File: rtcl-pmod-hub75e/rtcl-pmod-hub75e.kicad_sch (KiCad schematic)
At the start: 18 parts, among them J1 PMOD, J2 HIF3FC-16PA-2.54DSA(71), U1 74LVC273, U2 74LVC273, U3 74LVC273, U4 74LVC273, U5 LM809M3-2.93, U6 74LVC2G86

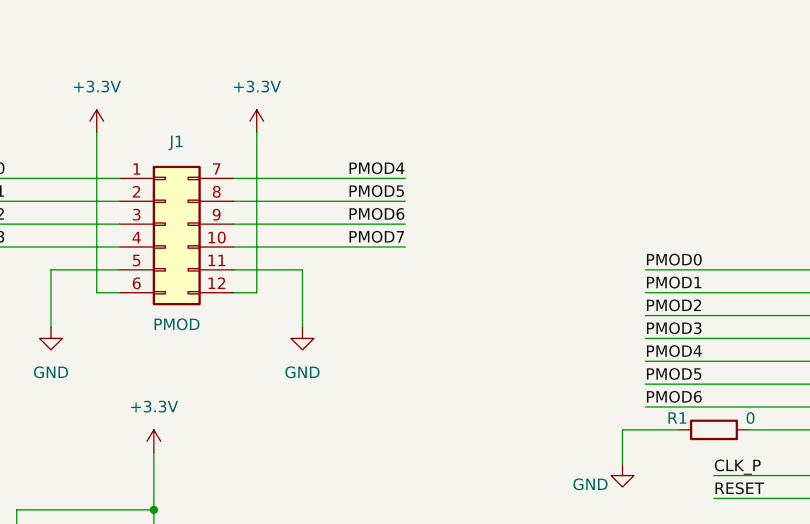
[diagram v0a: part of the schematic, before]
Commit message: Update .gitignore and modify schematic for power symbols and designators
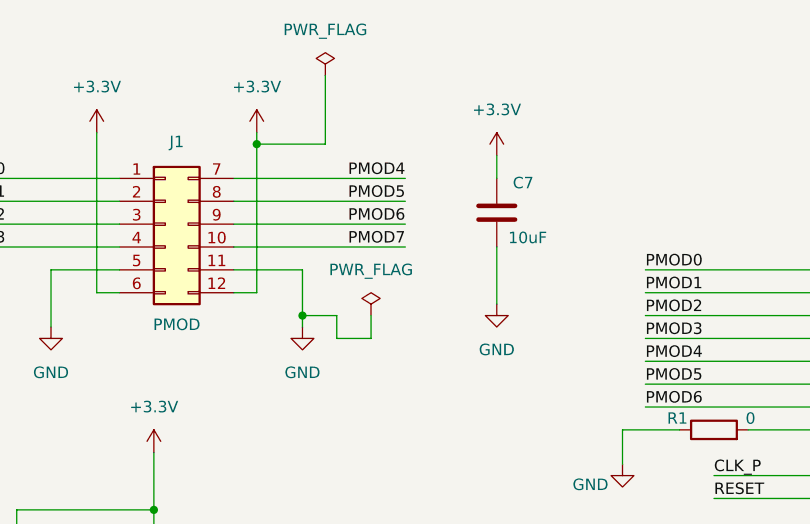
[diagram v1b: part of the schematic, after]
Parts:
- added C7: 10uF, symbol Device:C
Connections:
- net +3.3V: now also C7.1
- net GND: now also C7.2

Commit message: Add footprints for PH_02x06_2.54mm and PH_02x08_2.54mm headers; update existing schematic properties
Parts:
- C1, C2, C3, C4, C5, C6, C7: footprint (none) -> Capacitor_SMD:C_0603_1608Metric
- J1: footprint (none) -> rtcl-pmod-hub75e:PH_02x06_2.54mm
- J2: footprint (none) -> rtcl-pmod-hub75e:PH_02x08_2.54mm
- R1, R2: footprint (none) -> Resistor_SMD:R_0603_1608Metric
- TP1, TP2: footprint (none) -> TestPoint:TestPoint_Pad_2.0x2.0mm
- U1, U2, U3, U4: footprint (none) -> Package_SO:TSSOP-20_4.4x6.5mm_P0.65mm
- U5: LCSC (none) -> C414611
- U6: footprint (none) -> Package_SO:VSSOP-8_2.3x2mm_P0.5mm; LCSC (none) -> C507252
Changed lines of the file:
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@@
 			)
 		)
-		(property "Footprint" ""
+		(property "Footprint" "Package_SO:TSSOP-20_4.4x6.5mm_P0.65mm"
 			(at 181.61 129.54 0)
 			(hide yes)
@@
 			)
 		)
-		(property "Footprint" ""
+		(property "Footprint" "Resistor_SMD:R_0603_1608Metric"
 			(at 111.76 136.398 90)
 			(hide yes)
@@
 			)
 		)
-		(property "Footprint" ""
+		(property "Footprint" "TestPoint:TestPoint_Pad_2.0x2.0mm"
 			(at 207.01 134.62 0)
 			(hide yes)
@@
 			)
 		)
-		(property "Footprint" ""
+		(property "Footprint" "Package_SO:TSSOP-20_4.4x6.5mm_P0.65mm"
 			(at 137.16 129.54 0)
 			(hide yes)
@@
 			)
 		)
-		(property "Footprint" ""
+		(property "Footprint" "Package_SO:TSSOP-20_4.4x6.5mm_P0.65mm"
 			(at 181.61 60.96 0)
 			(hide yes)
@@
 			)
 		)
-		(property "Footprint" ""
+		(property "Footprint" "Capacitor_SMD:C_0603_1608Metric"
 			(at 130.5052 107.95 0)
 			(hide yes)
@@
 			)
 		)
-		(property "Footprint" ""
+		(property "Footprint" "Capacitor_SMD:C_0603_1608Metric"
 			(at 174.9552 39.37 0)
 			(hide yes)
@@
 			)
 		)
-		(property "Footprint" ""
+		(property "Footprint" "Capacitor_SMD:C_0603_1608Metric"
 			(at 174.9552 107.95 0)
 			(hide yes)
@@
 			)
 		)
-		(property "Footprint" ""
+		(property "Footprint" "Package_SO:TSSOP-20_4.4x6.5mm_P0.65mm"
 			(at 137.16 60.96 0)
 			(hide yes)
@@
 			)
 		)
-		(property "Footprint" ""
+		(property "Footprint" "Capacitor_SMD:C_0603_1608Metric"
 			(at 36.5252 135.89 0)
 			(hide yes)
@@
 			)
 		)
+		(property "LCSC" "C414611"
+			(at 50.8 90.17 0)
+			(hide yes)
+			(show_name no)
+			(do_not_autoplace no)
+			(effects
+				(font
+					(size 1.27 1.27)
+				)
+			)
+		)
 		(pin "3"
 		)
@@
 			)
 		)
-		(property "Footprint" ""
+		(property "Footprint" "Package_SO:VSSOP-8_2.3x2mm_P0.5mm"
 			(at 83.82 185.42 0)
 			(hide yes)
@@
 			)
 		)
+		(property "LCSC" "C507252"
+			(at 83.82 185.42 0)
+			(hide yes)
+			(show_name no)
+			(do_not_autoplace no)
+			(effects
+				(font
+					(size 1.27 1.27)
+				)
+			)
+		)
 		(pin "6"
 		)
@@
 			)
 		)
-		(property "Footprint" ""
+		(property "Footprint" "Capacitor_SMD:C_0603_1608Metric"
 			(at 89.8652 45.72 0)
 			(hide yes)
@@
 			)
 		)
-		(property "Footprint" ""
+		(property "Footprint" "Capacitor_SMD:C_0603_1608Metric"
 			(at 36.5252 87.63 0)
 			(hide yes)
@@
 			)
 		)
-		(property "Footprint" ""
+		(property "Footprint" "Package_SO:VSSOP-8_2.3x2mm_P0.5mm"
 			(at 50.8 135.89 0)
 			(hide yes)
@@
 			)
 		)
+		(property "LCSC" "C507252"
+			(at 50.8 135.89 0)
+			(hide yes)
+			(show_name no)
+			(do_not_autoplace no)
+			(effects
+				(font
+					(size 1.27 1.27)
+				)
+			)
+		)
 		(pin "6"
 		)
@@
 			)
 		)
-		(property "Footprint" ""
+		(property "Footprint" "Resistor_SMD:R_0603_1608Metric"
 			(at 113.03 67.818 90)
 			(hide yes)
@@
 			)
 		)
-		(property "Footprint" ""
+		(property "Footprint" "Capacitor_SMD:C_0603_1608Metric"
 			(at 130.5052 39.37 0)
 			(hide yes)
@@
 			)
 		)
-		(property "Footprint" ""
+		(property "Footprint" "TestPoint:TestPoint_Pad_2.0x2.0mm"
 			(at 207.01 66.04 0)
 			(hide yes)
@@
 			)
 		)
-		(property "Footprint" ""
+		(property "Footprint" "Package_SO:VSSOP-8_2.3x2mm_P0.5mm"
 			(at 83.82 168.91 0)
 			(hide yes)
@@
 			)
 		)
+		(property "LCSC" "C507252"
+			(at 83.82 168.91 0)
+			(hide yes)
+			(show_name no)
+			(do_not_autoplace no)
+			(effects
+				(font
+					(size 1.27 1.27)
+				)
+			)
+		)
 		(pin "2"
 		)
@@
 			)
 		)
-		(property "Footprint" ""
+		(property "Footprint" "rtcl-pmod-hub75e:PH_02x08_2.54mm"
 			(at 241.3 92.71 0)
 			(hide yes)
@@
 			)
 		)
-		(property "Footprint" ""
+		(property "Footprint" "rtcl-pmod-hub75e:PH_02x06_2.54mm"
 			(at 52.07 43.18 0)
 			(hide yes)

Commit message: Refactor code structure for improved readability and maintainability
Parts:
- removed TP1, TP2: Conn_01x01, TestPoint:TestPoint_Pad_2.0x2.0mm, symbol Connector_Generic:Conn_01x01
- added J3: Conn_01x02, Connector_PinHeader_2.54mm:PinHeader_1x02_P2.54mm_Vertical, symbol Connector_Generic:Conn_01x02
- added TP1, TP2, TP3, TP4: TestPoint, TestPoint:TestPoint_Pad_D1.0mm, symbol Connector:TestPoint
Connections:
- net +3.3V: now also J3.1 (Pin_1)
- net GND: now also J3.2 (Pin_2)
- net PMOD0: now also U2.8 (D3); no longer U2.3 (D0)
- net PMOD1: now also U2.7 (D2); no longer U2.4 (D1)
- net PMOD2: now also U2.4 (D1); no longer U2.7 (D2)
- net PMOD3: now also U2.3 (D0); no longer U2.8 (D3)
- net PMOD4: now also U1.17 (D6); no longer U1.13 (D4)
- net PMOD6: now also U1.13 (D4); no longer U1.17 (D6)
- net D4N: now reaches U2.12 (Q4), U4.13 (D4)
- net D5N: now reaches U2.15 (Q5), U4.14 (D5)
- net D6N: now reaches U2.16 (Q6), U4.17 (D6)
- net D7N: now reaches U2.19 (Q7), U4.18 (D7)
- net at U4.19 (Q7): now also TP2.1
- net D0N: now reaches U2.2 (Q0), U4.3 (D0)
- net D1N: now reaches U2.5 (Q1), U4.4 (D1)
- net D2N: now reaches U2.6 (Q2), U4.7 (D2)
- net D3N: now reaches U2.9 (Q3), U4.8 (D3)
- net at R2.2, U2.18 (D7): now also TP4.1
- net D4P: now reaches U1.12 (Q4), U3.13 (D4)
- net D5P: now reaches U1.15 (Q5), U3.14 (D5)
- net D6P: now reaches U1.16 (Q6), U3.17 (D6)
- net D7P: now reaches U1.19 (Q7), U3.18 (D7)
- net at U3.19 (Q7): now also TP1.1
- net D0P: now reaches U1.2 (Q0), U3.3 (D0)
- net D1P: now reaches U1.5 (Q1), U3.4 (D1)
- net D2P: now reaches U1.6 (Q2), U3.7 (D2)
- net D3P: now reaches U1.9 (Q3), U3.8 (D3)
- net at R1.2, U1.18 (D7): now also TP3.1
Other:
- moved on the sheet: C3, C4, J2, R1, U3, U4

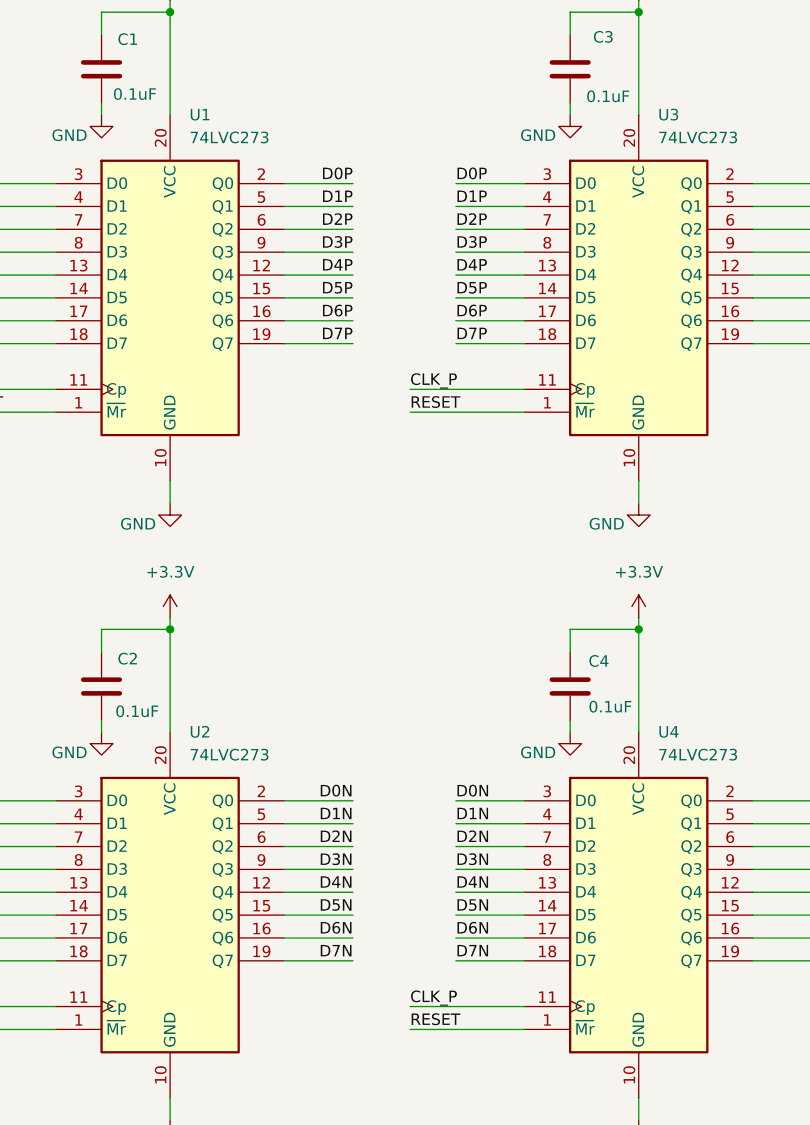
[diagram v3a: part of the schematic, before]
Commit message: Update PCB design parameters and wire connections in the rtcl-pmod-hub75e project
- Changed active layer from 0 to 2 in the project settings.
- Cleared used designators in the project file for better clarity.
- Adjusted multiple wire connection points in the schematic to correct coordinates for improved layout.
- Updated label positions for various components to reflect new wire connections and ensure proper alignment.
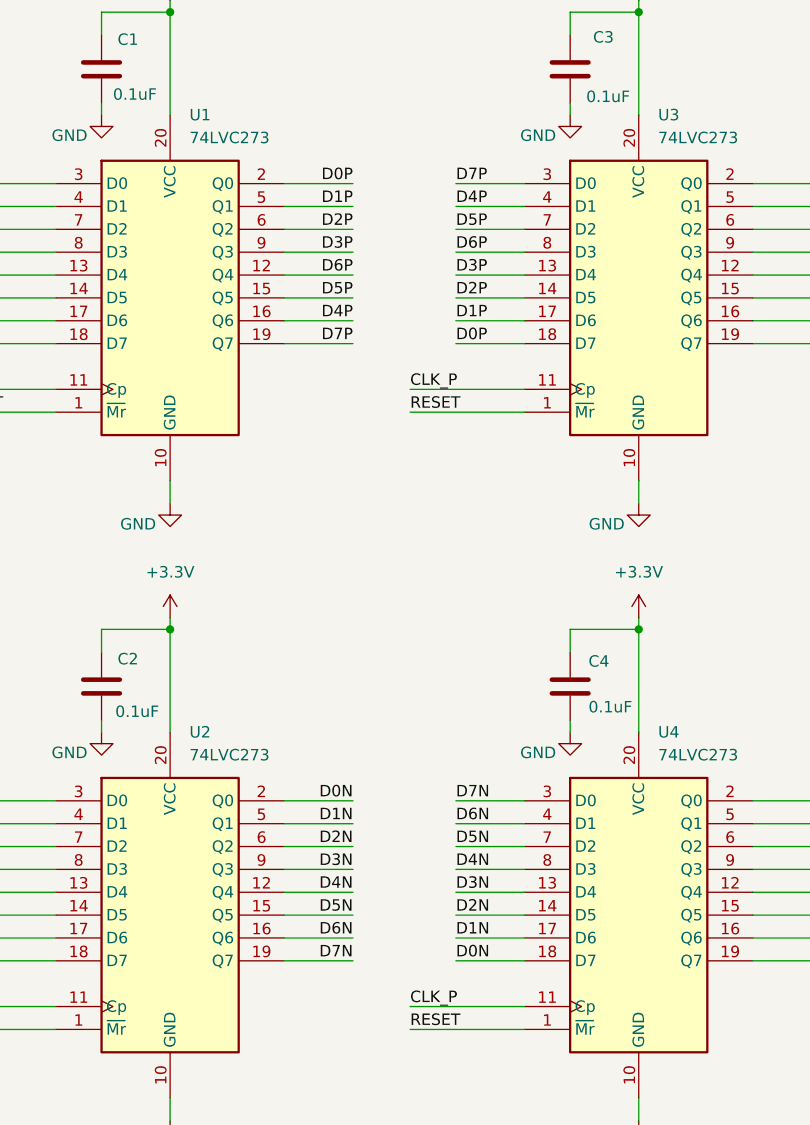
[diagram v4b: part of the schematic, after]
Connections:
- net D0N: now also U4.18 (D7); no longer U4.3 (D0)
- net D0P: now also U3.18 (D7); no longer U3.3 (D0)
- net D1N: now also U4.17 (D6); no longer U4.4 (D1)
- net D1P: now also U3.17 (D6); no longer U3.4 (D1)
- net D2N: now also U4.14 (D5); no longer U4.7 (D2)
- net D2P: now also U3.14 (D5); no longer U3.7 (D2)
- net D3N: now also U4.13 (D4); no longer U4.8 (D3)
- net D3P: now also U3.13 (D4); no longer U3.8 (D3)
- net D4N: now also U4.8 (D3); no longer U4.13 (D4)
- net D4P: now also U1.16 (Q6), U3.4 (D1); no longer U1.12 (Q4), U3.13 (D4)
- net D5N: now also U4.7 (D2); no longer U4.14 (D5)
- net D5P: now also U3.7 (D2); no longer U3.14 (D5)
- net D6N: now also U4.4 (D1); no longer U4.17 (D6)
- net D6P: now also U1.12 (Q4), U3.8 (D3); no longer U1.16 (Q6), U3.17 (D6)
- net D7N: now also U4.3 (D0); no longer U4.18 (D7)
- net D7P: now also U3.3 (D0); no longer U3.18 (D7)
